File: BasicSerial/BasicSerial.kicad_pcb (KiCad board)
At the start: 2 copper layers, 99.9 x 99.9 mm, 7 parts, among them J1 IDE_CONNECTOR, J2 CF Adapter Power, J3 Bus_ISA_8bit

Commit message: BasicSerial: Place DB-9 connector.
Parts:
- added C1: 0.1uF, Capacitor_THT:C_Disc_D5.1mm_W3.2mm_P5.00mm, F.Cu at (79.4, 66.0)
- added C2: 0.1uF, Capacitor_THT:C_Disc_D5.1mm_W3.2mm_P5.00mm, F.Cu at (13.9, 115.3)
- added C3: 0.1uF, Capacitor_THT:C_Disc_D5.1mm_W3.2mm_P5.00mm, F.Cu at (51.7, 97.2)
- added C4: 0.1uF, Capacitor_THT:C_Disc_D5.1mm_W3.2mm_P5.00mm, F.Cu at (42.0, 104.4)
- added C5: 22uF, Capacitor_THT:CP_Radial_D7.5mm_P2.50mm, F.Cu at (74.1, 83.0)
- added C6: 22pF, Capacitor_THT:C_Disc_D5.0mm_W2.5mm_P5.00mm, F.Cu at (55.3, 92.8)
- added C7: 56pF, Capacitor_THT:C_Disc_D5.0mm_W2.5mm_P5.00mm, F.Cu at (58.0, 88.1)
- added CN1: DB9_Male, w_conn_d-sub:DB_9M, F.Cu at (196.7, 86.1)
- added J1: COM_SELECT, 00Custom:PinHeader_3x02_P2.54mm_Vertical, F.Cu at (42.7, 97.1)
- added J2: IRQ_SELECT, Connector_PinHeader_2.54mm:PinHeader_2x05_P2.54mm_Vertical, F.Cu at (72.9, 66.0)
- added R1: 1.5K, Resistor_THT:R_Axial_DIN0207_L6.3mm_D2.5mm_P10.16mm_Horizontal, F.Cu at (42.0, 92.8)
- added R2: 1M, Resistor_THT:R_Axial_DIN0207_L6.3mm_D2.5mm_P10.16mm_Horizontal, F.Cu at (58.0, 84.0)
- added R3: 1M, Resistor_THT:R_Axial_DIN0207_L6.3mm_D2.5mm_P10.16mm_Horizontal, F.Cu at (25.7, 87.9)
- added U1: 16550, Package_DIP:DIP-40_W15.24mm_Socket, F.Cu at (-4.99, 65.8)
- added U2: 1.8432 MHz, 00Custom:Crystal_DIP8_DIP14, F.Cu at (28.4, 95.1)
- added U3: 74LS688 or GAL16V8, Package_DIP:DIP-20_W7.62mm_Socket, F.Cu at (14.4, 88.0)
- added U4: GD75232N, Package_DIP:DIP-20_W7.62mm_Socket, F.Cu at (46.8, 65.8)
- added Y1: 1.8432 MHz, Crystal:Crystal_HC49-U_Horizontal, F.Cu at (61.1, 65.2)
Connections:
- net -5V renamed Net-(J3-Pad5)
- net A10 renamed Net-(J3-Pad52)
- net A11 renamed Net-(J3-Pad51)
- net A12 renamed Net-(J3-Pad50)
- net A13 renamed Net-(J3-Pad49)
- net A14 renamed Net-(J3-Pad48)
- net A15 renamed Net-(J3-Pad47)
- net A16 renamed Net-(J3-Pad46)
- net A17 renamed Net-(J3-Pad45)
- net A18 renamed Net-(J3-Pad44)
- net A19 renamed Net-(J3-Pad43)
- net ALE renamed Net-(J3-Pad28)
- net CLK renamed Net-(J3-Pad20)
- net DRQ1 renamed Net-(J3-Pad18)
- net DRQ2 renamed Net-(J3-Pad6)
- net DRQ3 renamed Net-(J3-Pad16)
- net IOCHRDY renamed Net-(J3-Pad41)
- net IRQ6 renamed Net-(J3-Pad22)
- net OSC renamed Net-(J3-Pad30)
- net TC renamed Net-(J3-Pad27)
- net ~DACK0 renamed Net-(J3-Pad19)
- net ~DACK1 renamed Net-(J3-Pad17)
- net ~DACK2 renamed Net-(J3-Pad26)
- net ~DACK3 renamed Net-(J3-Pad15)
- net ~IO_CH_CK renamed Net-(J3-Pad32)
- net ~MEMR renamed Net-(J3-Pad12)
- net ~MEMW renamed Net-(J3-Pad11)

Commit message: BasicSerial: Initial layout work.
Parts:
- removed the J1 at (42.7, 97.1)
- removed the J1 at (167.6, 59.8)
- removed the J2 at (72.9, 66.0)
- removed the J2 at (174.3, 59.8)
- removed MH1, MH2, MH3, MH4: MH, MountingHole:MountingHole_3.5mm_Pad
- added J1: COM_SELECT, 00Custom:PinHeader_3x02_P2.54mm_Vertical, F.Cu at (109.9, 87.0)
- added J2: IRQ_SELECT, Connector_PinHeader_2.54mm:PinHeader_2x05_P2.54mm_Vertical, F.Cu at (119.4, 119.4)
- U2: value 1.8432 MHz -> 74LS688 or GAL16V8; footprint 00Custom:Crystal_DIP8_DIP14 -> Package_DIP:DIP-20_W7.62mm_Socket
- U3: value 74LS688 or GAL16V8 -> GD75232N
- U4: value GD75232N -> 1.8432 MHz; footprint Package_DIP:DIP-20_W7.62mm_Socket -> 00Custom:Crystal_DIP8_DIP14
- moved R3 146.8 mm to (170.8, 109.9), turned to 270 degrees
- moved U3 145.8 mm to (160.0, 80.0), turned to 90 degrees
- moved U1 144.8 mm to (134.6, 104.1), turned to 90 degrees
- moved Y1 129.6 mm to (179.7, 117.5), turned to 90 degrees
- moved R1 128.6 mm to (167.6, 120.0), turned to 90 degrees
- moved C6 123.7 mm to (177.2, 113.7), turned to 90 degrees
- moved C7 122.6 mm to (177.2, 116.8), turned to 270 degrees
- moved R2 118.8 mm to (174.0, 109.9), turned to 270 degrees
- moved U4 113.4 mm to (146.7, 119.4), turned to 90 degrees
- moved C3 107.4 mm to (156.2, 72.4), turned to 270 degrees
- moved C4 99.3 mm to (141.0, 111.8), turned to 270 degrees
- moved C2 92.2 mm to (104.1, 96.5), turned to 270 degrees
- moved U2 80.0 mm to (108.0, 104.1), turned to 90 degrees
- moved C1 56.3 mm to (130.8, 88.9), turned to 270 degrees
- moved C5 46.7 mm to (104.8, 118.1), turned to 180 degrees
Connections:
- U2 pad 1: VCC -> AEN
- U2 pad 11: VCC -> A06
- U2 pad 4: GND -> A03
- U2 pad 7: GND -> Net-(J1-Pad2)
- U2 pad 8: UART_XIN -> A05
- U3 pad 1: AEN -> +12V
- U3 pad 10: GND -> -12V
- U3 pad 11: A06 -> GND
- U3 pad 12: VCC -> Net-(U1-Pad39)
- U3 pad 13: A07 -> Net-(U1-Pad33)
- U3 pad 14: VCC -> Net-(U1-Pad36)
- U3 pad 15: A08 -> Net-(U1-Pad11)
- U3 pad 16: Net-(J1-Pad5) -> Net-(U1-Pad32)
- U3 pad 17: A09 -> Net-(U1-Pad10)
- U3 pad 18: VCC -> Net-(U1-Pad37)
- U3 pad 19: ~UART_CS -> Net-(U1-Pad38)
- U3 pad 2: GND -> Net-(CN1-Pad1)
- U3 pad 3: GND -> Net-(CN1-Pad6)
- U3 pad 4: A03 -> Net-(CN1-Pad2)
- U3 pad 5: VCC -> Net-(CN1-Pad7)
- U3 pad 6: A04 -> Net-(CN1-Pad3)
- U3 pad 7: Net-(J1-Pad2) -> Net-(CN1-Pad8)
- U3 pad 8: A05 -> Net-(CN1-Pad4)
- U3 pad 9: VCC -> Net-(CN1-Pad9)
- U4 pad 1: +12V -> VCC
- U4 pad 11: GND -> VCC
- U4 pad 14: Net-(U1-Pad36) -> VCC
- U4 pad 4: Net-(CN1-Pad2) -> GND
- U4 pad 7: Net-(CN1-Pad8) -> GND
- U4 pad 8: Net-(CN1-Pad4) -> UART_XIN
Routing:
- net Net-(CN1-Pad1): track 0.00 -> 30.6 mm
- net Net-(CN1-Pad6): track 0.00 -> 30.0 mm
- net Net-(CN1-Pad2): track 0.00 -> 24.4 mm
- net Net-(CN1-Pad7): track 0.00 -> 23.8 mm
- net Net-(CN1-Pad3): track 0.00 -> 18.1 mm
- net Net-(CN1-Pad8): track 0.00 -> 17.6 mm
- net Net-(CN1-Pad4): track 0.00 -> 11.9 mm
- net Net-(CN1-Pad9): track 0.00 -> 11.3 mm
- net GND: track 0.00 -> 7.62 mm, vias 0 -> 1
- added copper zone on B.Cu, net GND
- added copper zone on F.Cu, net GND

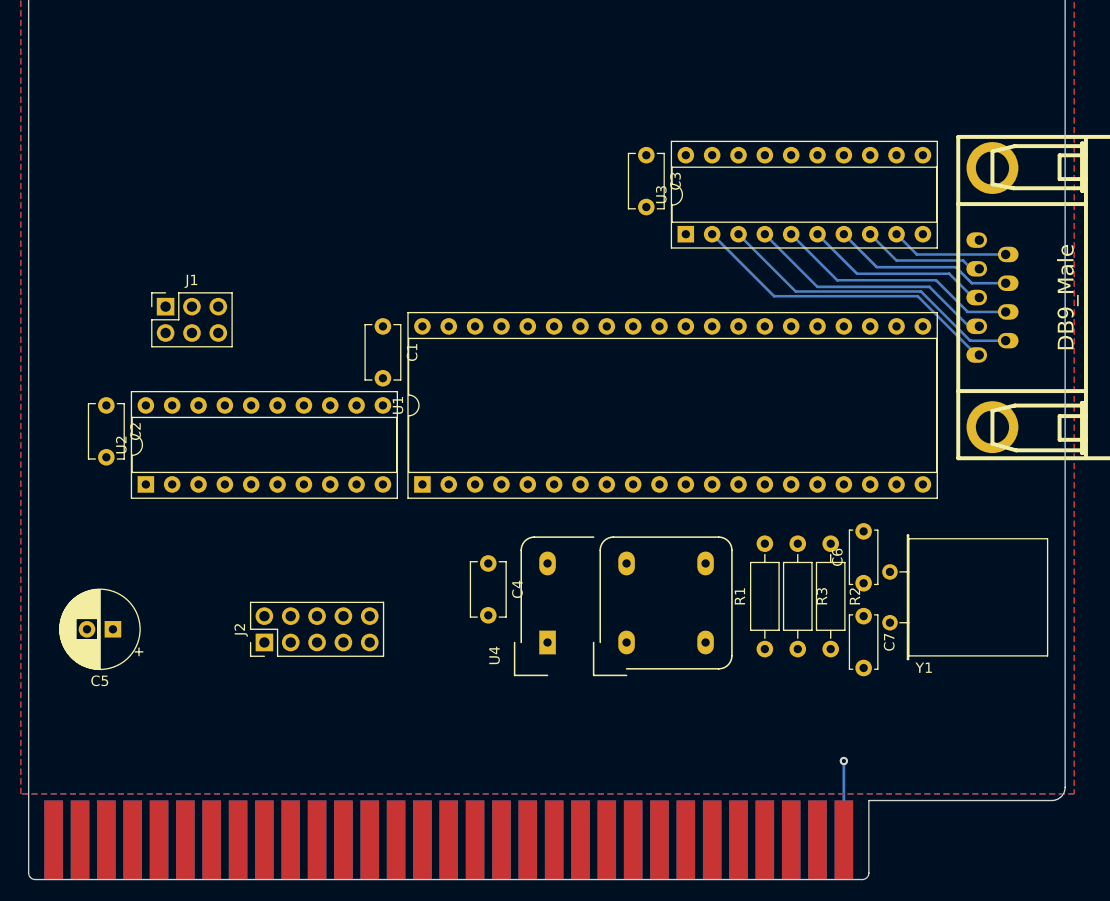
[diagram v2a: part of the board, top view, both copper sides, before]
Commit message: BasicSerial: Remove discrete oscillator option, re-organize the IC layout.
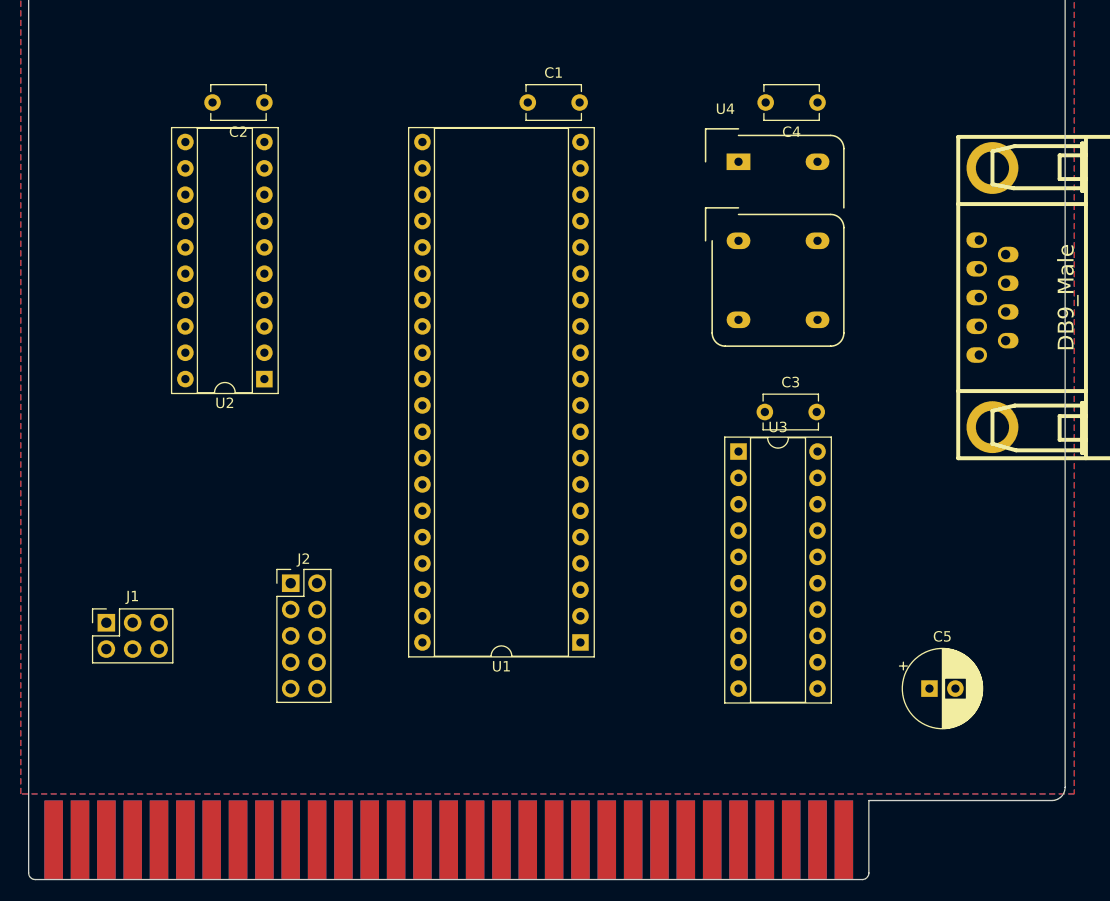
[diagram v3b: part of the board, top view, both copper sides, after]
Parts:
- removed C6: 22pF, Capacitor_THT:C_Disc_D5.0mm_W2.5mm_P5.00mm
- removed C7: 56pF, Capacitor_THT:C_Disc_D5.0mm_W2.5mm_P5.00mm
- removed R1: 1.5K, Resistor_THT:R_Axial_DIN0207_L6.3mm_D2.5mm_P10.16mm_Horizontal
- removed R2, R3: 1M, Resistor_THT:R_Axial_DIN0207_L6.3mm_D2.5mm_P10.16mm_Horizontal
- removed Y1: 1.8432 MHz, Crystal:Crystal_HC49-U_Horizontal
- moved C5 78.9 mm to (183.5, 123.8), turned to 0 degrees
- moved C4 54.6 mm to (172.7, 67.3), turned to 180 degrees
- moved U4 49.9 mm to (165.1, 73.0), turned to 0 degrees
- moved C2 32.9 mm to (119.4, 67.3), turned to 180 degrees
- moved J1 31.0 mm to (104.1, 117.5)
- moved C3 27.3 mm to (167.6, 97.2), turned to 0 degrees
- moved C1 25.7 mm to (144.8, 67.3), turned to 0 degrees
- moved U3 21.6 mm to (165.1, 101.0), turned to 0 degrees
- moved U1 21.6 mm to (149.9, 119.4), turned to 180 degrees
- moved U2 15.3 mm to (119.4, 94.0), turned to 180 degrees
- moved J2 6.25 mm to (121.9, 113.7), turned to 0 degrees
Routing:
- net Net-(CN1-Pad1): track 30.6 -> 0.00 mm
- net Net-(CN1-Pad6): track 30.0 -> 0.00 mm
- net Net-(CN1-Pad2): track 24.4 -> 0.00 mm
- net Net-(CN1-Pad7): track 23.8 -> 0.00 mm
- net Net-(CN1-Pad3): track 18.1 -> 0.00 mm
- net Net-(CN1-Pad8): track 17.6 -> 0.00 mm
- net Net-(CN1-Pad4): track 11.9 -> 0.00 mm
- net Net-(CN1-Pad9): track 11.3 -> 0.00 mm
- net GND: track 7.62 -> 0.00 mm, vias 1 -> 0

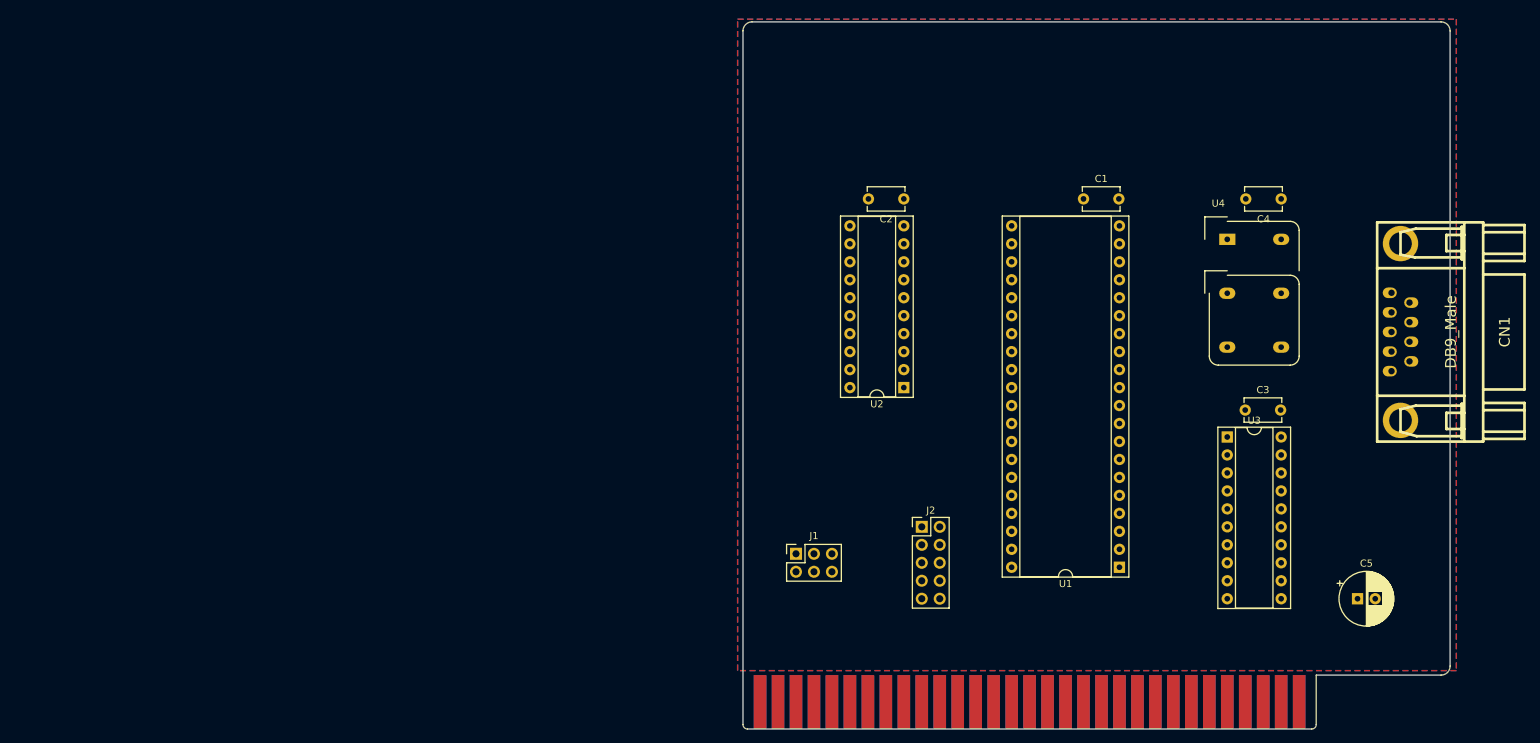
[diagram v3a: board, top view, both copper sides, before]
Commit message: BasicSerial: Reduce size of board so it is only as tall as needed by the serial connector.
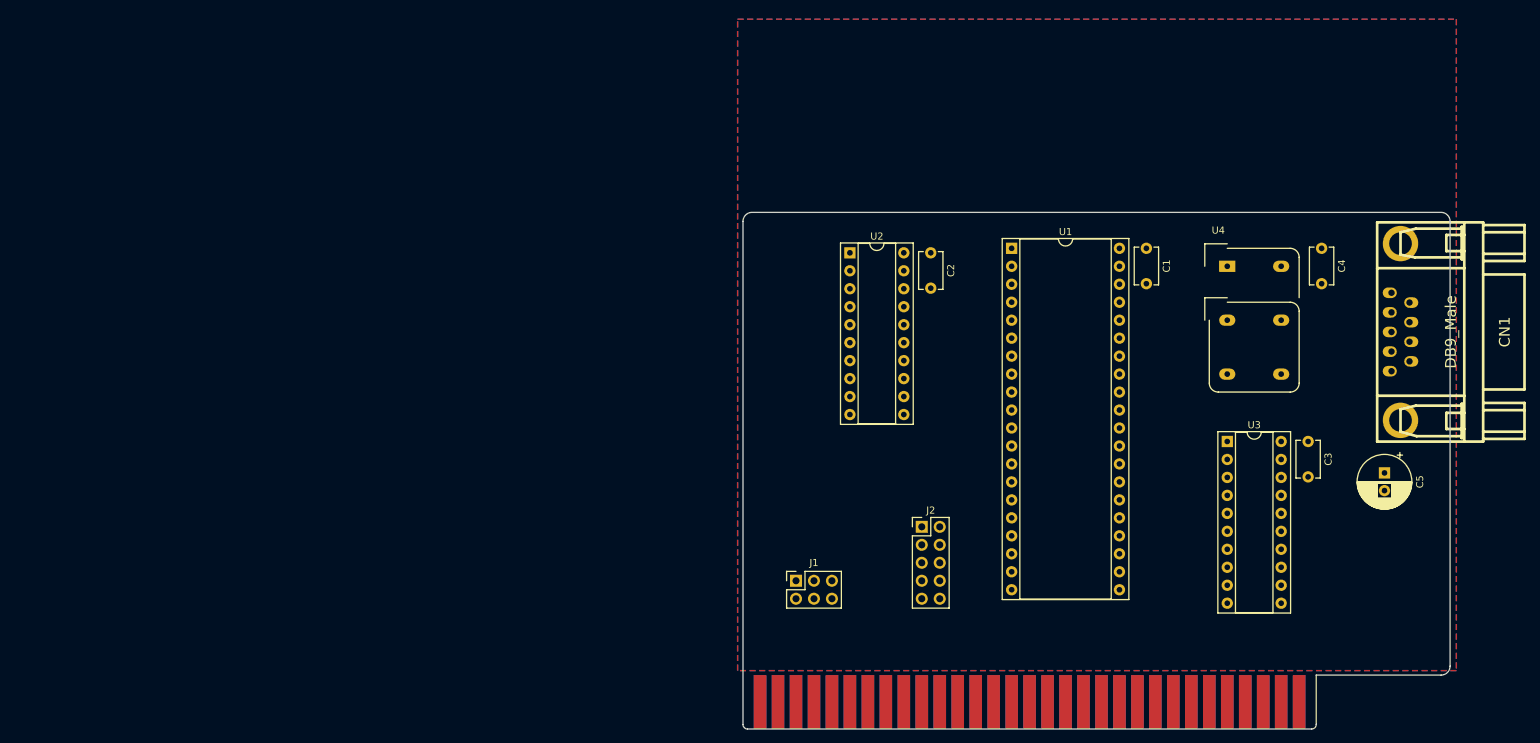
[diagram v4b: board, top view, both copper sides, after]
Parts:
- moved U1 47.6 mm to (134.6, 74.3), turned to 0 degrees
- moved U2 20.5 mm to (111.8, 74.9), turned to 0 degrees
- moved C5 18.2 mm to (187.3, 106.0), turned to 270 degrees
- moved C1 11.3 mm to (153.7, 74.3), turned to 270 degrees
- moved C3 9.94 mm to (176.5, 101.6), turned to 270 degrees
- moved C4 9.03 mm to (178.4, 74.3), turned to 270 degrees
- moved C2 8.52 mm to (123.2, 74.9), turned to 270 degrees
- moved J1 3.81 mm to (104.1, 121.3)
- moved U4 3.81 mm to (165.1, 76.8)
- moved U3 0.63 mm to (165.1, 101.6)
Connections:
- CN1 pad : (no net) -> GND
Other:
- board size 99.9 x 99.9 mm -> 99.9 x 73 mm

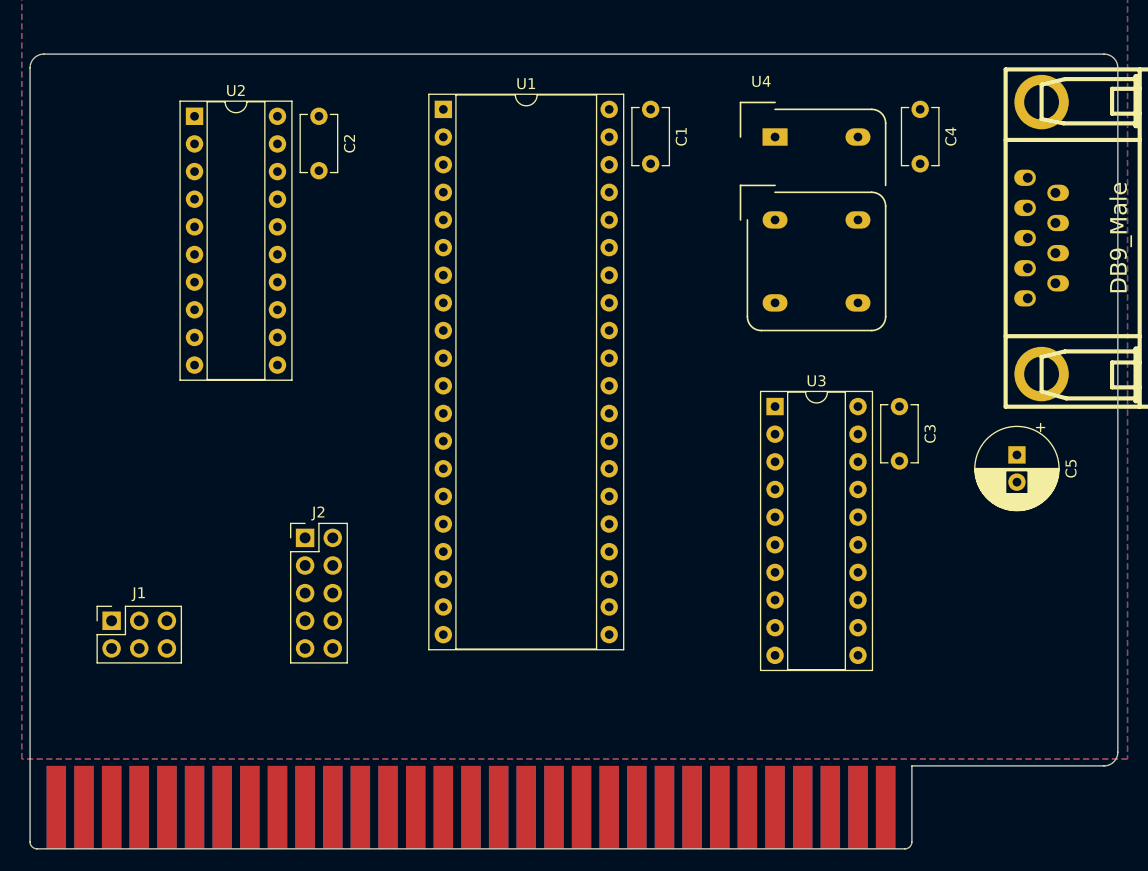
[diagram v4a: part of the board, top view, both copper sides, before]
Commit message: Basic Serial: Add +-12v decoupling caps. WIP on board routing.
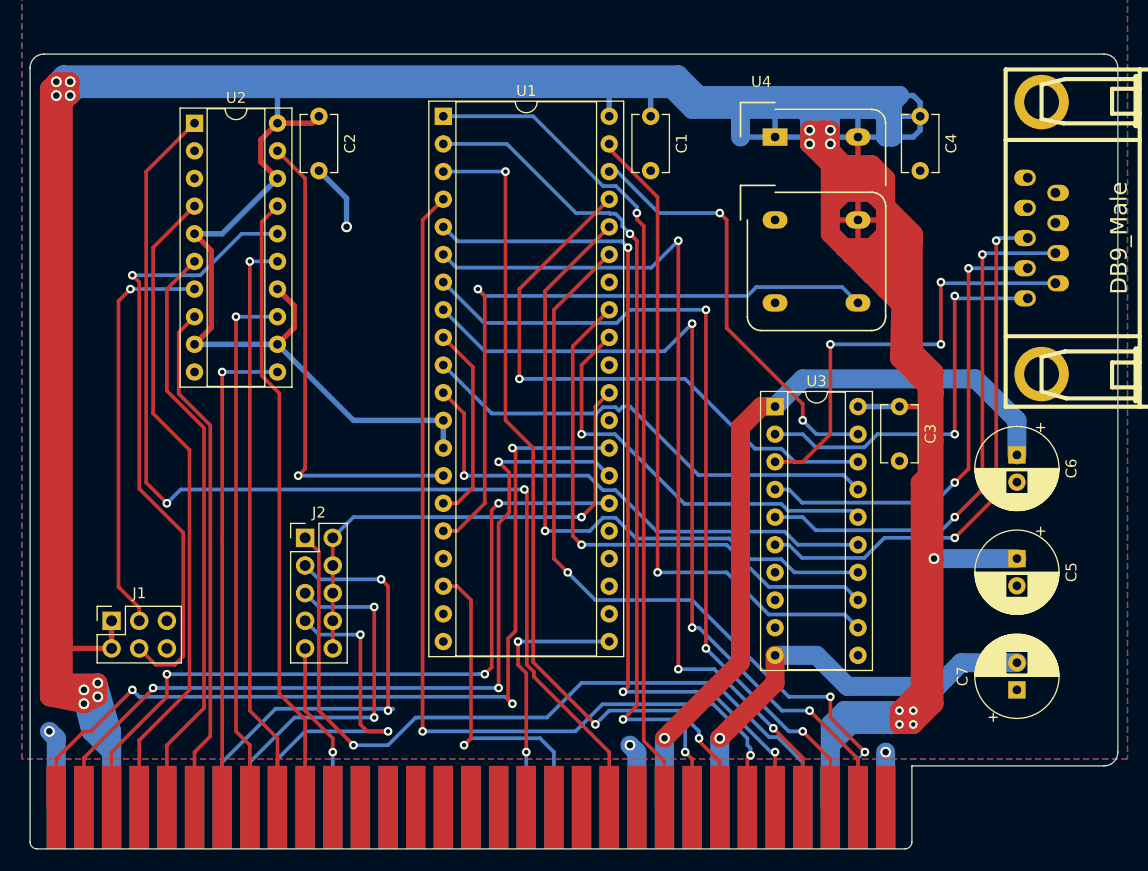
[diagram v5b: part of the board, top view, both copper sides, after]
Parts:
- added C6: 4.7uF, Capacitor_THT:CP_Radial_D7.5mm_P2.50mm, F.Cu at (187.3, 106.0)
- added C7: 4.7uF, Capacitor_THT:CP_Radial_D7.5mm_P2.50mm, F.Cu at (187.3, 127.6)
- moved C5 9.52 mm to (187.3, 115.6)
- moved C1 0.64 mm to (153.7, 74.9)
- moved C4 0.64 mm to (178.4, 74.9)
- moved U1 0.64 mm to (134.6, 74.9)
- moved U2 0.63 mm to (111.8, 75.6)
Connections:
- net Net-(CN1-Pad1) renamed /SER_PIN1
- net Net-(CN1-Pad2) renamed /SER_PIN2
- net Net-(CN1-Pad3) renamed /SER_PIN3
- net Net-(CN1-Pad4) renamed /SER_PIN4
- net Net-(CN1-Pad6) renamed /SER_PIN6
- net Net-(CN1-Pad7) renamed /SER_PIN7
- net Net-(CN1-Pad8) renamed /SER_PIN8
- net Net-(CN1-Pad9) renamed /SER_PIN9
- J2 pad 2: IRQ3 -> Net-(J2-Pad10)
- J2 pad 3: IRQ4 -> IRQ3
- J2 pad 4: IRQ5 -> Net-(J2-Pad10)
- J2 pad 5: IRQ7 -> IRQ4
- J2 pad 7: Net-(J2-Pad10) -> IRQ5
- J2 pad 9: Net-(J2-Pad10) -> IRQ7
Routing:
- net VCC: track 0.00 -> 697.0 mm, vias 0 -> 17
- net AEN: track 0.00 -> 103.4 mm, vias 0 -> 2
- net D3: track 0.00 -> 88.4 mm, vias 0 -> 2
- net A00: track 0.00 -> 82.5 mm, vias 0 -> 3
- net D5: track 0.00 -> 81.9 mm, vias 0 -> 3
- net D4: track 0.00 -> 80.1 mm, vias 0 -> 3
- net D1: track 0.00 -> 80.0 mm, vias 0 -> 3
- net D2: track 0.00 -> 78.5 mm, vias 0 -> 3
- net D7: track 0.00 -> 78.1 mm, vias 0 -> 3
- net A01: track 0.00 -> 77.6 mm, vias 0 -> 3
- net D0: track 0.00 -> 77.5 mm, vias 0 -> 1
- net D6: track 0.00 -> 77.4 mm, vias 0 -> 3
- net RESET: track 0.00 -> 72.4 mm, vias 0 -> 3
- net IRQ2: track 0.00 -> 71.7 mm, vias 0 -> 1
- net A02: track 0.00 -> 69.9 mm, vias 0 -> 3
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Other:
- net class Default: clearance 0.2 -> 0.24; trace_width 0.25 -> 0.34
- net class Power added: clearance 0.24, trace_width 0.5, via_dia 1, via_drill 0.6
- net class Power High V added: clearance 0.48, trace_width 0.5, via_dia 1, via_drill 0.6
- net class Serial added: clearance 0.46, trace_width 0.34, via_dia 0.8, via_drill 0.4
- rule trace_clearance: 0.2 -> 0.24
